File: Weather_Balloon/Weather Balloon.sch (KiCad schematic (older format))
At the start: 13 parts

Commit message: Logging packed
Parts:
- removed C? (x3): 22uF, symbol C
- removed C? (x3): 1nF, symbol C
- removed P?: CONN_01X10, symbol CONN_01X10
- added C?: 0.1uF, symbol C
- added IC?: ATTINY85-P, DIP8, symbol ATTINY85-P
- added P?: 2560_RESET, symbol CONN_01X02
- added P?: SERIAL, symbol CONN_01X02
- added P?: SCK, symbol CONN_01X02
- added P?: MOSI, symbol CONN_01X02
- added P?: MISO, symbol CONN_01X02
- added P?: Geiger, symbol CONN_01X05
- added Q?: MPS2222A, symbol Q_NPN_EBC
- added R?: 100, symbol R
- added R? (x2): 10k, symbol R
- added R?: 4.7k, symbol R
- added U?: BILEVEL_SHIFT, symbol BILEVEL_SHIFT
- Y?: value 8Mhz -> 16Mhz
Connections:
- net +3V3: now also Q?.3 (C), U?.10 (LVcc); no longer C?.1, C?.1, IC?.10 (VCC), IC?.100 (AVCC), IC?.31 (VCC), IC?.80 (VCC)
- net Custom_Heat: now also IC?.5 ((OC3A/AIN1)PE3)
- net GND: now also C?.1, C?.1, C?.1, P?.2 (P2), R?.2, U?.4 (GND), U?.9 (GND); no longer C?.2, C?.2
- net GPS_Heat: now also IC?.17 (PH5(OC4C))
- net Light_Heat: now also IC?.18 (PH6(OC2B))
- net Main_Heat: now also IC?.15 (PH3(OC4A))
- net UV_Heat: now also IC?.16 (PH4(OC4B))
- net at IC?.2 ((PCINT8/RXD0)PE0): now also P?.1 (P1)
- net at IC?.20 ((PCINT1/SCK)PB1): now also P?.1 (P1)
- net at IC?.21 ((PCINT2/MOSI)PB2): now also P?.1 (P1)
- net at IC?.22 ((PCINT3/MISO)PB3): now also P?.1 (P1)
- net at IC?.3 ((TXD0)PE1): now also P?.2 (P2)
- net at IC?.30 (~RESET): now also P?.1 (P1)
- net SCL_5: now reaches IC?.43 ((SCL/INT0)PD0)
- net SCL_5: now also U?.1 (HV1)
- net SDA_5: now reaches IC?.44 ((SDA/INT1)PD1)
- net SDA_5: now also U?.2 (HV2)
- net at IC?.45 ((RXD1/INT2)PD2): now also U?.5 (HV3)
- net at IC?.46 ((TXD1/INT3)PD3): now also U?.6 (HV4)
- net Humidity_Heat: now reaches IC?.6 ((OC3B/INT4)PE4)
- net at IC?.63 (PJ0(RXD3/PCINT9)): now also P?.5 (P5)
- net at IC?.64 (PJ1(TXD3/PCINT10)): now also P?.3 (P3)
- net at IC?.65 (PJ2(XCK3/PCINT11)): now also P?.1 (P1)
- net LANDING_LED: now reaches IC?.74 ((AD4)PA4)
- net PIEZO: now reaches IC?.75 ((AD3)PA3)
- net PIEZO_PWR: now reaches IC?.76 ((AD2)PA2)
- net DS18B20_DATA: now reaches IC?.77 ((AD1)PA1)
- net DS18B20_PWR: now reaches IC?.78 ((AD0)PA0)
- net at IC?.82 (PK7(ADC15/PCINT23)): now also R?.1
- net UV_VOLTAGE: now reaches IC?.96 ((ADC1)PF1)
- net UV_POWER: now reaches IC?.97 ((ADC0)PF0)
- new net: C?.2, C?.2, IC?.100 (AVCC), R?.2
- new net: P?.4 (P4), Q?.1 (E)
- new net: Q?.2 (B), R?.1, R?.2
- new net +5V: R?.1, R?.2, U?.3 (HVcc)
- new net 2560_RESET: C?.2, P?.2 (P2), R?.1
- new net GPS_RX: U?.8 (LV3)
- new net GPS_TX: U?.7 (LV4)
- new net MISO: P?.2 (P2)
- new net MOSI: P?.2 (P2)
- new net SCK: P?.2 (P2)
- new net SCL_3.3: U?.12 (LV1)
- new net SDA_3.3: U?.11 (LV2)
- new net Vcc_1: IC?.10 (VCC)
- new net Vcc_2: IC?.31 (VCC)
- new net Vcc_3: IC?.80 (VCC)
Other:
- moved on the sheet: C?, IC?, Y?

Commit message: Initial PCB design with throughhole components. Layout not finilized.
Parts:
- removed P?: Geiger, symbol CONN_01X05
- removed Q?: MPS2222A, symbol Q_NPN_EBC
- removed R?: 4.7k, symbol R
- removed R?: 10k, symbol R
- added C10, C11, C5: 10pF, Capacitors_SMD:C_1206_HandSoldering, symbol C
- added C4: 22uF, Capacitors_Tantalum_SMD:TantalC_SizeC_EIA-6032_HandSoldering, symbol C
- added C8, C9: 0.1uF, Capacitors_SMD:C_1206_HandSoldering, symbol C
- added D1: Green, Personal:LED-5MM, symbol Led_Small
- added D2: Yellow, Personal:LED-5MM, symbol Led_Small
- added D3: Red, Personal:LED-5MM, symbol Led_Small
- added P1: 85_PRGM, Personal:Pin_Header_Straight_1x05, symbol CONN_01X05
- added P22: RADIO, Personal:Pin_Header_Straight_1x10_BACK, symbol CONN_01X10
- added P8: 85_RESET, Personal:Pin_Header_Straight_1x02, symbol CONN_01X02
- added R3, R9: 10k, Resistors_ThroughHole:Resistor_Horizontal_RM10mm, symbol R
- added R4, R43, R44, R45, R46, R47, R6: 4.7k, Resistors_ThroughHole:Resistor_Horizontal_RM10mm, symbol R
- added R5, R7, R8: 150, Resistors_ThroughHole:Resistor_Horizontal_RM10mm, symbol R
- added R53, R54, R55, R56, R57, R58, R59, R60, R61, R62, R63, R64, R65, R66, R67: 22, Resistors_ThroughHole:Resistor_Horizontal_RM10mm, symbol R
- added SW1: SILENCE, Buttons_Switches_ThroughHole:SW_PUSH-12mm, symbol SW_PUSH_SMALL_H
- added U1: MAX6107EUR, TO_SOT_Packages_SMD:SOT-23_Handsoldering, symbol MAX6107EUR
- C1: renamed from C?; footprint (none) -> Capacitors_Tantalum_SMD:TantalC_SizeC_EIA-6032_HandSoldering
- C2: renamed from C?; footprint (none) -> Capacitors_SMD:C_1206_HandSoldering
- C3: renamed from C?; value 1nF -> 10pF; footprint (none) -> Capacitors_SMD:C_1206_HandSoldering
- C6, C7: renamed from C?; footprint (none) -> Capacitors_ThroughHole:C_Disc_D3_P2.5
- IC1: renamed from IC?; footprint DIP8 -> Housings_DIP:DIP-8_W7.62mm_LongPads
- IC2: renamed from IC?; footprint TQFP100 -> Housings_QFP:TQFP-100_14x14mm_Pitch0.5mm
- P10, P4: renamed from P?; footprint (none) -> Personal:Pin_Header_Straight_1x02
- P5: renamed from P?; value SCK -> 2560_SCK; footprint (none) -> Personal:Pin_Header_Straight_1x02
- P6: renamed from P?; value MOSI -> 2560_MOSI; footprint (none) -> Personal:Pin_Header_Straight_1x02
- P7: renamed from P?; value MISO -> 2560_MISO; footprint (none) -> Personal:Pin_Header_Straight_1x02
- R1, R2: renamed from R?; footprint (none) -> Resistors_ThroughHole:Resistor_Horizontal_RM10mm
- U2: renamed from U?; footprint (none) -> Personal:DIP-12_W7.62mm_LongPads_BACK
- Y1: renamed from Y?; footprint (none) -> Personal:HC-49V
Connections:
- net Light_Heat is gone; now on net GPS_Heat: IC2.18 (PH6(OC2B))
- net +3V3: now also C11.1, R46.1, R47.1
- net +5V: now also IC1.8 (VCC), C10.1, C4.2, C5.2, C9.1, P1.5 (P5), P22.1 (P1), R3.1, R4.1, R43.1, R44.1, R45.1, R5.1, R6.1, R7.1, R8.1, SW1.2, U1.1 (VCC)
- net 2560_RESET: now also IC1.2 (PB3(XTAL1/CLKI/OC1B/ADC3/PCINT3))
- net AREF: now also U1.2 (OUT)
- net Custom_Heat: now also IC2.15 (PH3(OC4A)); no longer IC2.5 ((OC3A/AIN1)PE3)
- net GND: now also IC1.4 (GND), C10.2, C11.2, C4.1, C5.1, C8.2, C9.2, P1.4 (P4), P22.10 (P10), R9.2, U1.3 (GND)
- net GPS_Heat: no longer IC2.17 (PH5(OC4C))
- net MISO: now also R4.2
- net MOSI: now also R6.2
- net Main_Heat: now also IC2.16 (PH4(OC4B)); no longer IC2.15 (PH3(OC4A))
- net SCL_3.3: now also R47.2, R65.1; no longer U2.12 (LV1)
- net SCL_5: now also R45.2, R64.1; no longer IC2.43 ((SCL/INT0)PD0)
- net SDA_3.3: now also R46.2, R67.1; no longer U2.11 (LV2)
- net SDA_5: now also R44.2, R66.1; no longer IC2.44 ((SDA/INT1)PD1)
- net UV_Heat: now also IC2.17 (PH5(OC4C)); no longer IC2.16 (PH4(OC4B))
- net UV_POWER: now also IC2.35 (PL0(ICP4)); no longer IC2.97 ((ADC0)PF0)
- net UV_VOLTAGE: now also IC2.97 ((ADC0)PF0); no longer IC2.96 ((ADC1)PF1)
- net AT25_CS_9: now reaches IC2.12 (PH0(RXD2))
- net AT25_CS_8: now reaches IC2.13 (PH1(TXD2))
- net AT25_CS_7: now reaches IC2.14 (PH2(XCK2))
- net at IC2.19 ((PCINT0/~SS~)PB0): now also R53.2
- net at IC2.20 ((PCINT1/SCK)PB1): now also R54.2; no longer P5.1 (P1)
- net at IC2.21 ((PCINT2/MOSI)PB2): now also R56.2; no longer P6.1 (P1)
- net at IC2.24 ((PCINT5/OC1A)PB5): now also D1.1 (K)
- net at IC2.25 ((PCINT6/OC1B)PB6): now also D2.1 (K)
- net at IC2.26 ((PCINT7/OC0A/OC1C)PB7): now also D3.1 (K)
- net AT25_CS_6: now reaches IC2.27 (PH7(T4))
- net AT25_CS_4: now reaches IC2.28 (PG3(TOSC2))
- net AT25_CS_5: now reaches IC2.29 (PG4(TOSC1))
- net SHT31_RESET: now reaches IC2.36 (PL1(ICP5))
- net DOF_POWER: now reaches IC2.37 (PL2(T5))
- net MS5607_POWER: now reaches IC2.38 (PL3(OC5A))
- net TSL2561_POWER: now reaches IC2.39 (PL4(OC5B))
- net SD_POWER: now reaches IC2.40 (PL5(OC5C))
- net GPS_POWER: now reaches IC2.41 (PL6)
- net GEIGER_POWER: now reaches IC2.42 (PL7)
- net AT25_CS_1: now reaches IC2.51 (PG0(~WR~))
- net AT25_CS_2: now reaches IC2.52 (PG1(~RD~))
- net RADIO_0: now reaches IC2.53 ((A8)PC0)
- net RADIO_0: now also R55.2
- net RADIO_1: now reaches IC2.54 ((A9)PC1)
- net RADIO_1: now also R57.2
- net RADIO_2: now reaches IC2.55 ((A10)PC2)
- net RADIO_2: now also R58.2
- net RADIO_3: now reaches IC2.56 ((A11)PC3)
- net RADIO_3: now also R59.2
- net RADIO_4: now reaches IC2.57 ((A12)PC4)
- net RADIO_4: now also R60.2
- net RADIO_5: now reaches IC2.58 ((A13)PC5)
- net RADIO_5: now also R61.2
- net RADIO_6: now reaches IC2.59 ((A14)PC6)
- net RADIO_6: now also R62.2
- net RADIO_7: now reaches IC2.60 ((A15)PC7)
- net RADIO_7: now also R63.2
- net GEIGER_X: now reaches IC2.63 (PJ0(RXD3/PCINT9))
- net GEIGER_Y: now reaches IC2.64 (PJ1(TXD3/PCINT10))
- net GEIGER_Z: now reaches IC2.65 (PJ2(XCK3/PCINT11))
- net AT25_CS_3: now reaches IC2.70 (PG2(ALE))
- net 2560_HEARTBEAT: now reaches IC2.73 ((AD5)PA5)
- net 2560_HEARTBEAT: now also IC1.3 (PB4(XTAL2/CLKO/OC1B/ADC2/PCINT4))
- net AT25_CS_10: now reaches IC2.79 (PJ7)
- net at IC2.9 ((CLKO/ICP3/INT7)PE7): now also R9.1, SW1.1
- net at IC1.1 (PB5(~RESET~/dW/ADC0/PCINT5)): now also P8.1 (P1)
- net at IC1.5 (PB0(MOSI/DI/SDA/AIN0/OC0A/OC1A/AREF/PCINT0)): now also P1.3 (P3)
- net at IC1.6 (PB1(MISO/DO/AIN1/OC0B/OC1A/PCINT1)): now also P1.2 (P2)
- net at IC1.7 (PB2(SCK/USCK/SCL/T0/INT0/ADC1/PCINT2)): now also P1.1 (P1)
- net GPS_RX renamed 2560_RX_GPS_TX
- net GPS_TX renamed 2560_TX_GPS_RX
- net Humidity_Heat renamed TSL2561_Heat
- new net: IC2.43 ((SCL/INT0)PD0), R64.2
- new net: IC2.44 ((SDA/INT1)PD1), R66.2
- new net: R67.2, U2.11 (LV2)
- new net: R65.2, U2.12 (LV1)
- new net: P5.1 (P1), R54.1
- new net: P6.1 (P1), R56.1
- new net: C8.1, P8.2 (P2), R3.2
- new net: P22.2 (P2), R55.1
- new net: P22.3 (P3), R57.1
- new net: P22.4 (P4), R58.1
- new net: P22.5 (P5), R59.1
- new net: P22.6 (P6), R60.1
- new net: P22.7 (P7), R61.1
- new net: P22.8 (P8), R62.1
- new net: P22.9 (P9), R63.1
- new net: D1.2 (A), R5.2
- new net: D2.2 (A), R7.2
- new net: D3.2 (A), R8.2
- new net SHT31_Heat: IC2.5 ((OC3A/AIN1)PE3)
- new net SS: R43.2, R53.1
- no-connect marks 0 -> 30
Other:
- moved on the sheet: C1, C2, C3, C6, C7, IC1, IC2, P10, P4, P5, P6, P7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

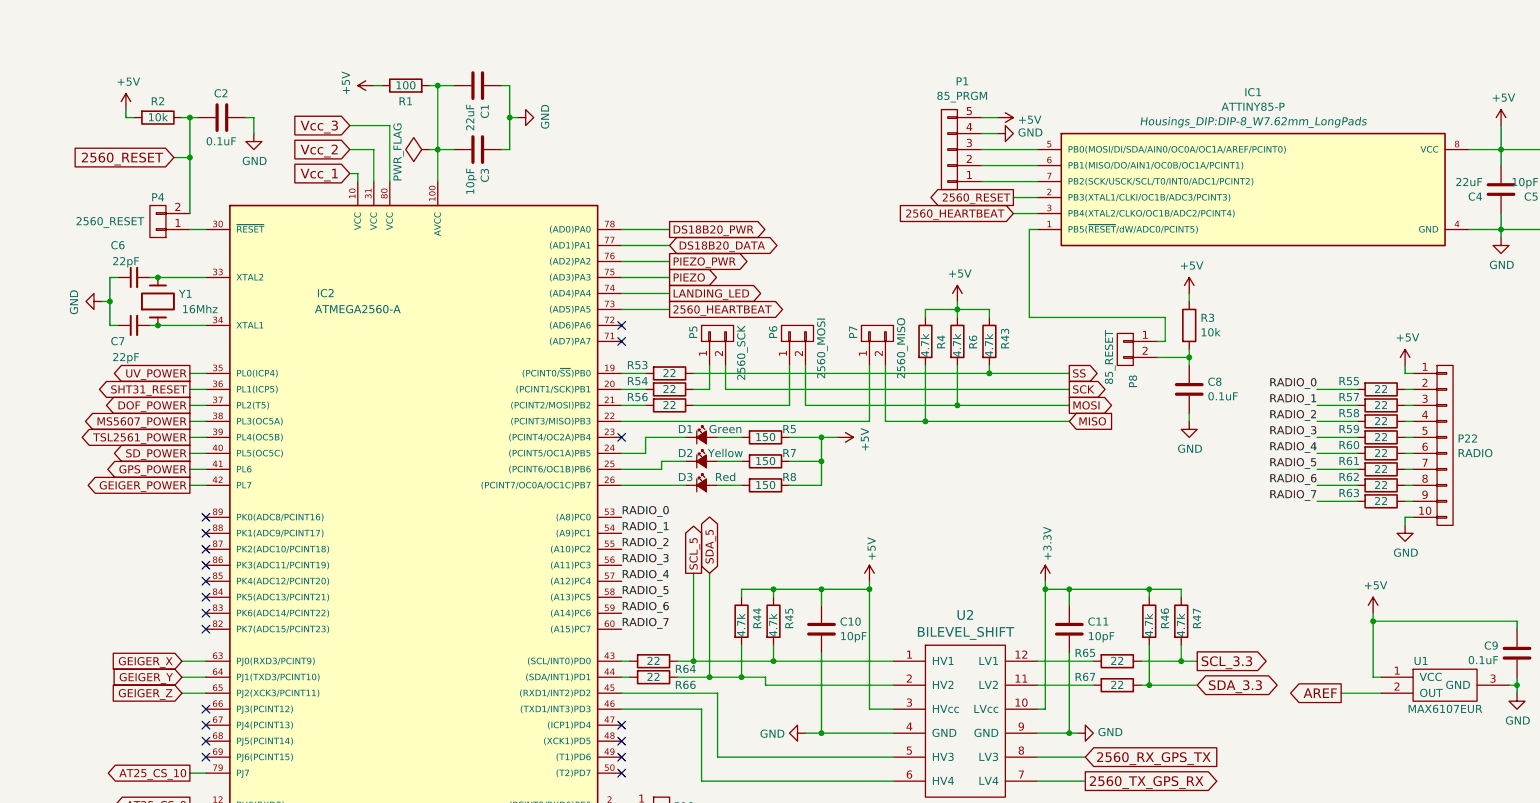
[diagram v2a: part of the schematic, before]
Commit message: Before manual trace width adjust
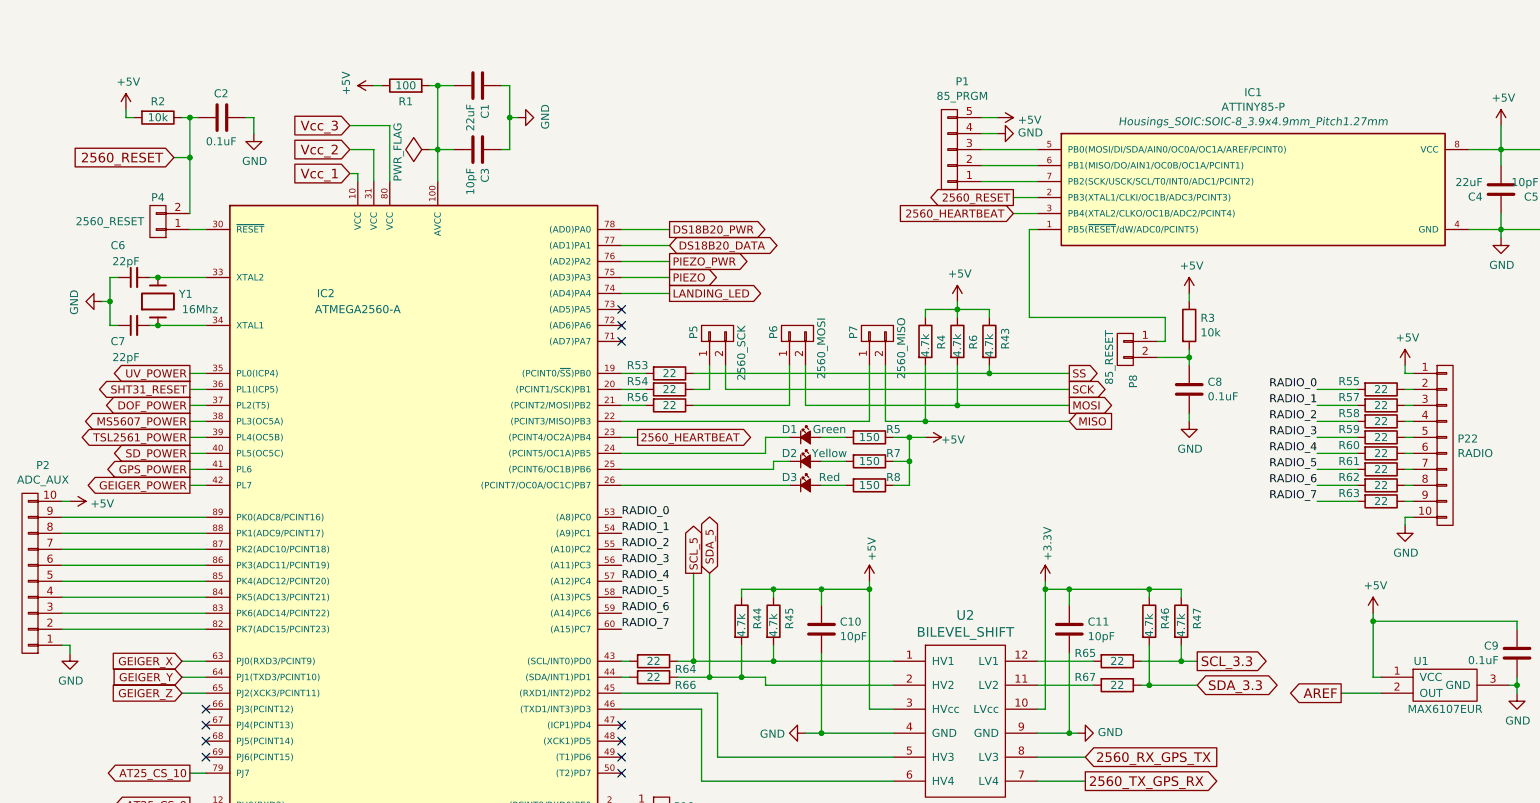
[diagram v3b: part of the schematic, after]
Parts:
- added P2: ADC_AUX, Pin_Headers:Pin_Header_Straight_1x10, symbol CONN_01X10
- D1, D2, D3: footprint Personal:LED-5MM -> LEDs:LED_1206
- IC1: footprint Housings_DIP:DIP-8_W7.62mm_LongPads -> Housings_SOIC:SOIC-8_3.9x4.9mm_Pitch1.27mm
- P1: footprint Personal:Pin_Header_Straight_1x05 -> Pin_Headers:Pin_Header_Straight_1x05
- P10, P4, P5, P6, P7, P8: footprint Personal:Pin_Header_Straight_1x02 -> Pin_Headers:Pin_Header_Straight_1x02
- P22: footprint Personal:Pin_Header_Straight_1x10_BACK -> Pin_Headers:Pin_Header_Straight_1x10
- R1, R2, R3, R4, R43, R44, R45, R46, R47, R5, R53, R54, R55, R56, R57, R58, R59, R6, R60, R61, R62, R63, R64, R65, R66, R67, R7, R8, R9: footprint Resistors_ThroughHole:Resistor_Horizontal_RM10mm -> Resistors_SMD:R_1206_HandSoldering
- U2: footprint Personal:DIP-12_W7.62mm_LongPads_BACK -> Personal:DIP-12_W7.62mm_LongPads_ALL
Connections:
- net +5V: now also P2.10 (P10)
- net 2560_HEARTBEAT: now also IC2.23 ((PCINT4/OC2A)PB4); no longer IC2.73 ((AD5)PA5)
- net GND: now also P2.1 (P1)
- net at IC2.82 (PK7(ADC15/PCINT23)): now also P2.2 (P2)
- net at IC2.83 (PK6(ADC14/PCINT22)): now also P2.3 (P3)
- net at IC2.84 (PK5(ADC13/PCINT21)): now also P2.4 (P4)
- net at IC2.85 (PK4(ADC12/PCINT20)): now also P2.5 (P5)
- net at IC2.86 (PK3(ADC11/PCINT19)): now also P2.6 (P6)
- net at IC2.87 (PK2(ADC10/PCINT18)): now also P2.7 (P7)
- net at IC2.88 (PK1(ADC9/PCINT17)): now also P2.8 (P8)
- net at IC2.89 (PK0(ADC8/PCINT16)): now also P2.9 (P9)
- no-connect marks 30 -> 22
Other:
- moved on the sheet: D1, D2, D3, R5, R7, R8
